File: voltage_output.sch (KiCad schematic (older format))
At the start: 29 parts, among them P2 BAN+, P3 BAN-, Q1 MMBT2369, SW3 SPDT, SW4 ROTARY 12POS

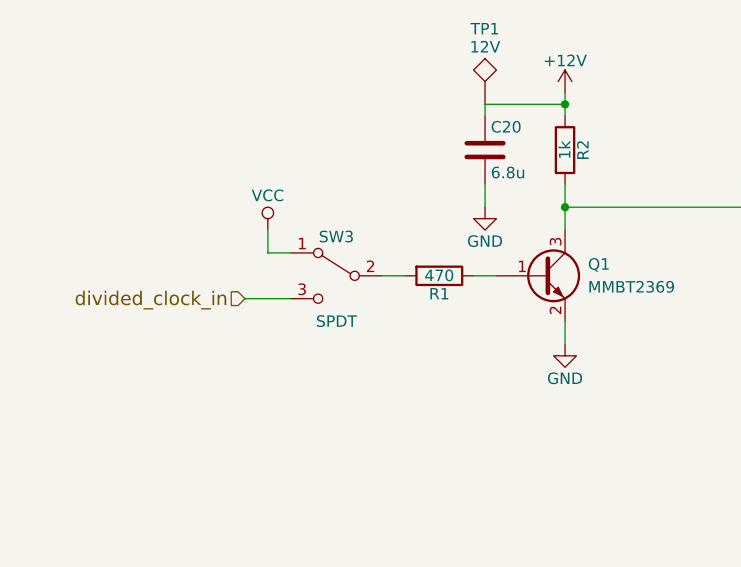
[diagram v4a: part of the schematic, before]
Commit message: Several schematic & layout changes after building first boards
- increase current limiting resistors on LEDs to make them less blinding
- add speedup cap, increase base resistor on voltage output switching
  transistor for better high frequency performance (should work up to 10MHz)
- change switched/constant voltage output toggle switch to actually work
  (now toggles between switched voltage output and constant voltage
  output, rather than switched and 0V output)
- add inverter to make div-by-5 circuit work
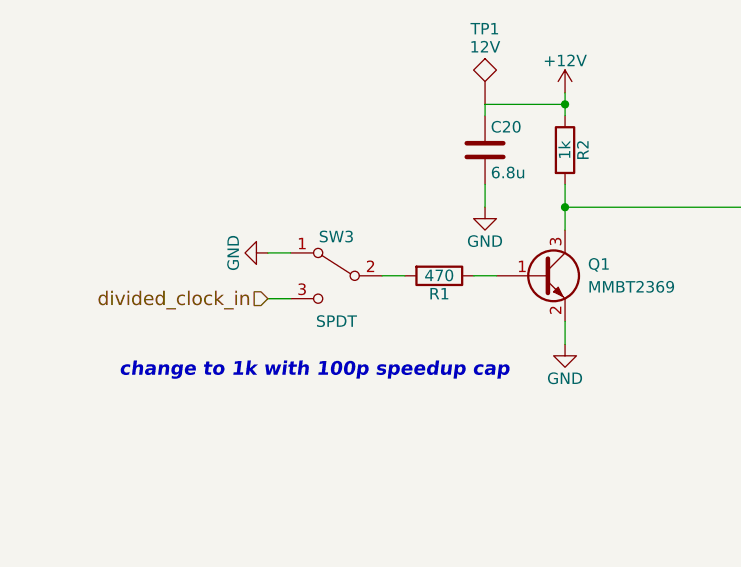
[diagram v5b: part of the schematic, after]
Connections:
- net VCC is gone; now on net GND: SW3.1 (A)
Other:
- note added: "change to 1k with 100p speedup cap"
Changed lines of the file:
@@
 $EndComp
 $Comp
-L GND #PWR063
+L GND #PWR065
 U 1 1 58C45C04
 P 5750 7350
-F 0 "#PWR063" H 5750 7100 50  0001 C CNN
+F 0 "#PWR065" H 5750 7100 50  0001 C CNN
 F 1 "GND" H 5750 7200 50  0000 C CNN
 F 2 "" H 5750 7350 50  0000 C CNN
@@
 $EndComp
 $Comp
-L GND #PWR064
+L GND #PWR066
 U 1 1 58C4A090
 P 9800 3100
-F 0 "#PWR064" H 9800 2850 50  0001 C CNN
+F 0 "#PWR066" H 9800 2850 50  0001 C CNN
 F 1 "GND" H 9800 2950 50  0000 C CNN
 F 2 "" H 9800 3100 50  0000 C CNN
@@
 	1    0    0    -1
 $EndComp
-Text HLabel 1300 2100 0    60   Input ~ 0
+Text HLabel 1400 2100 0    60   Input ~ 0
 divided_clock_in
 $Comp
@@
 $EndComp
 $Comp
-L +12V #PWR065
+L +12V #PWR067
 U 1 1 58C7B681
 P 2700 1200
-F 0 "#PWR065" H 2700 1050 50  0001 C CNN
+F 0 "#PWR067" H 2700 1050 50  0001 C CNN
 F 1 "+12V" H 2700 1340 50  0000 C CNN
 F 2 "" H 2700 1200 50  0000 C CNN
@@
 $EndComp
 $Comp
-L GND #PWR066
+L GND #PWR068
 U 1 1 58C7B717
 P 2700 2300
-F 0 "#PWR066" H 2700 2050 50  0001 C CNN
+F 0 "#PWR068" H 2700 2050 50  0001 C CNN
 F 1 "GND" H 2700 2150 50  0000 C CNN
 F 2 "" H 2700 2300 50  0000 C CNN
 F 3 "" H 2700 2300 50  0000 C CNN
 	1    2700 2300
-	1    0    0    -1
-$EndComp
-$Comp
-L VCC #PWR067
-U 1 1 58C7CD5D
-P 1400 1800
-F 0 "#PWR067" H 1400 1650 50  0001 C CNN
-F 1 "VCC" H 1400 1950 50  0000 C CNN
-F 2 "" H 1400 1800 50  0000 C CNN
-F 3 "" H 1400 1800 50  0000 C CNN
-	1    1400 1800
 	1    0    0    -1
 $EndComp
@@
 $EndComp
 $Comp
-L GND #PWR068
+L GND #PWR069
 U 1 1 58C9DDF5
 P 2350 1700
-F 0 "#PWR068" H 2350 1450 50  0001 C CNN
+F 0 "#PWR069" H 2350 1450 50  0001 C CNN
 F 1 "GND" H 2350 1550 50  0000 C CNN
 F 2 "" H 2350 1700 50  0000 C CNN
@@
 $EndComp
 Wire Wire Line
-	1400 1800 1400 1900
-Wire Wire Line
 	1400 1900 1500 1900
 Wire Wire Line
@@
 	4400 600  5750 600
 Connection ~ 2700 1700
-Wire Wire Line
-	1300 2100 1500 2100
 Wire Wire Line
 	2350 1700 2350 1600
@@
 Text Notes 7200 4550 0    60   ~ 0
 Resistors in divider all 0.1% tolerance
+$Comp
+L GND #PWR070
+U 1 1 58F2ED06
+P 1400 1900
+F 0 "#PWR070" H 1400 1650 50  0001 C CNN
+F 1 "GND" H 1400 1750 50  0000 C CNN
+F 2 "" H 1400 1900 50  0000 C CNN
+F 3 "" H 1400 1900 50  0000 C CNN
+	1    1400 1900
+	0    1    1    0
+$EndComp
+Wire Wire Line
+	1400 2100 1500 2100
+Text Notes 750  2450 0    60   Italic 12
+change to 1k with 100p speedup cap
 $EndSCHEMATC

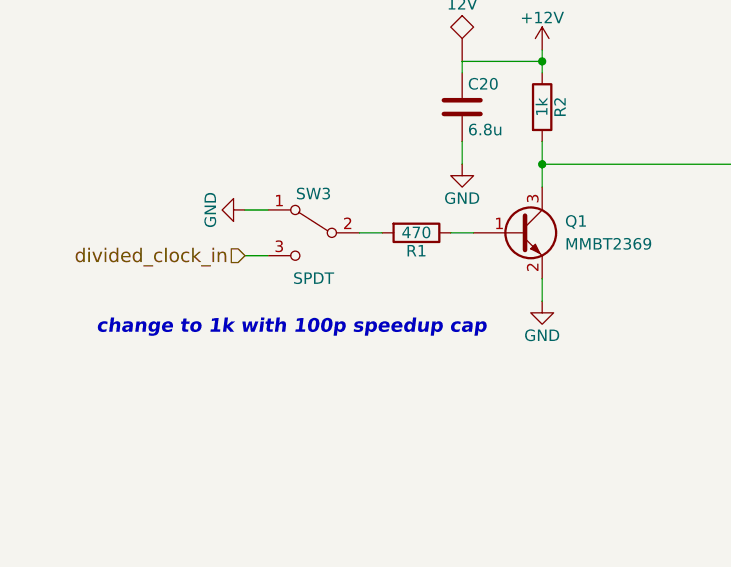
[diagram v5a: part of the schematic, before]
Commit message: update voltage output schematic
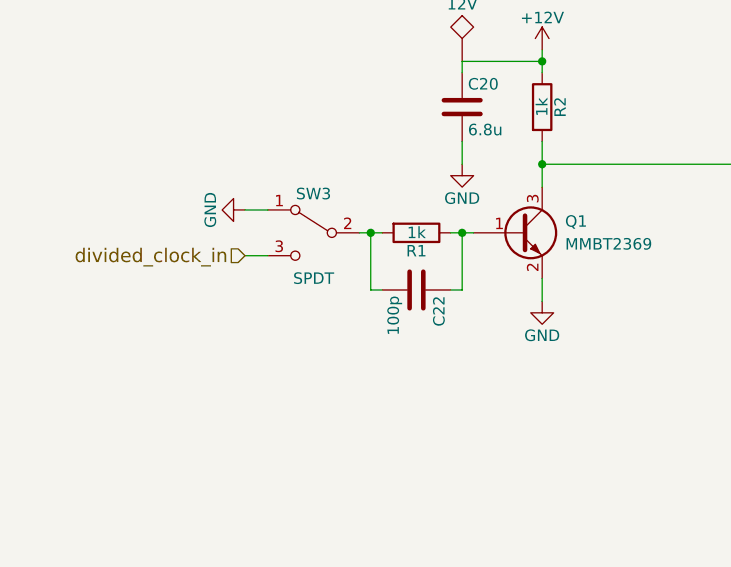
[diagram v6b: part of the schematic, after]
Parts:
- added C22: 100p, Capacitors_SMD:C_0805_HandSoldering, symbol C
- R1: value 470 -> 1k
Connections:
- net at R1.2, SW3.2 (B): now also C22.2
- net at Q1.1 (B), R1.1: now also C22.1
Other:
- note removed: "change to 1k with 100p speedup cap"
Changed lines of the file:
@@
 P 2150 2000
 F 0 "R1" V 2230 2000 50  0000 C CNN
-F 1 "470" V 2150 2000 50  0000 C CNN
+F 1 "1k" V 2150 2000 50  0000 C CNN
 F 2 "Resistors_SMD:R_0805_HandSoldering" V 2080 2000 50  0001 C CNN
 F 3 "" H 2150 2000 50  0000 C CNN
@@
 Wire Wire Line
 	1400 2100 1500 2100
-Text Notes 750  2450 0    60   Italic 12
-change to 1k with 100p speedup cap
+$Comp
+L C C22
+U 1 1 58F41F68
+P 2150 2250
+F 0 "C22" H 2175 2350 50  0000 L CNN
+F 1 "100p" H 2175 2150 50  0000 L CNN
+F 2 "Capacitors_SMD:C_0805_HandSoldering" H 2188 2100 50  0001 C CNN
+F 3 "" H 2150 2250 50  0000 C CNN
+	1    2150 2250
+	0    1    1    0
+$EndComp
+Wire Wire Line
+	1950 2000 1950 2250
+Wire Wire Line
+	1950 2250 2000 2250
+Connection ~ 1950 2000
+Wire Wire Line
+	2300 2250 2350 2250
+Wire Wire Line
+	2350 2250 2350 2000
+Connection ~ 2350 2000
 $EndSCHEMATC
